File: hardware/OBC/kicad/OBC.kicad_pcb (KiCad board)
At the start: 2 copper layers, 69.5 x 69.5 mm, 37 parts, among them J1 SOCKET_UP, J12 PLACA, J13 Conn_01x08_SocketMPU, J14 Conn_01x04_Socket, J15 Screw_Terminal_01x02, J16 Conn_01x02, J17 Conn_01x06_Socket, J18 Conn_01x02, J19 Conn_01x03, J21 Conn_01x02, J4 PLACA, J7 HEADER_DOWN, J8 PLACA, SW1 SW_SPDT, U1 25CSM04xxSN

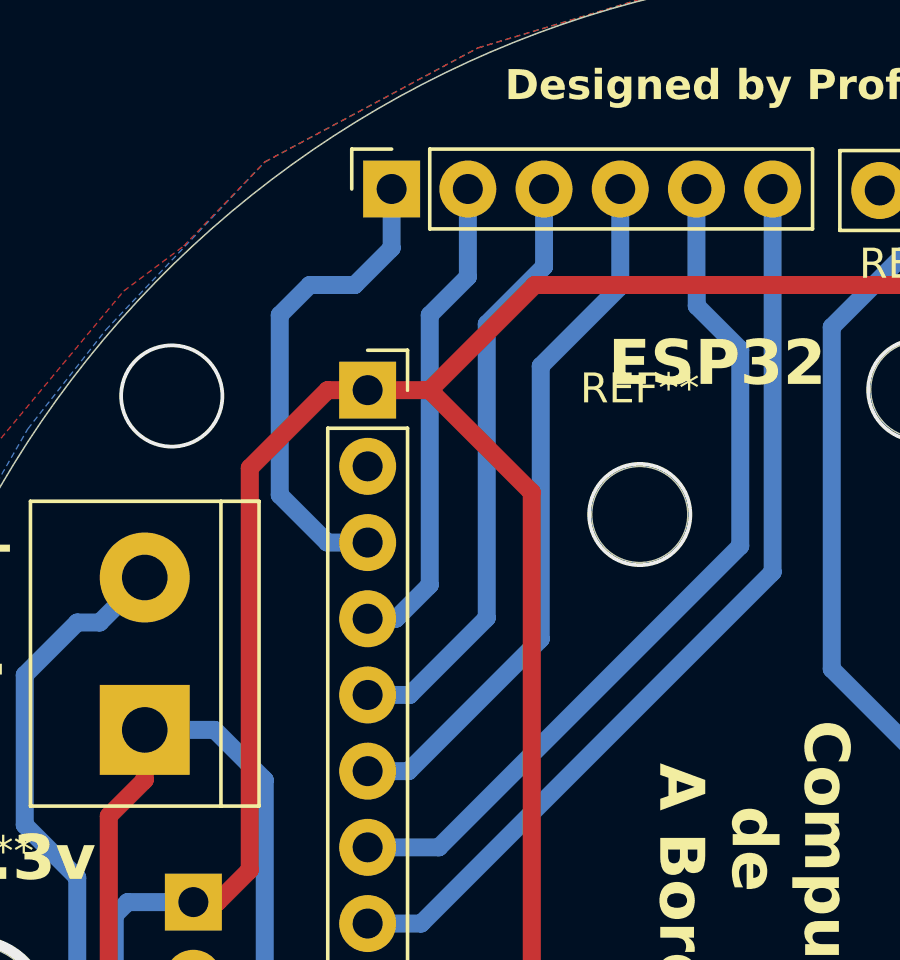
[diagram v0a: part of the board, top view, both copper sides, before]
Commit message: First actualization for OBC PCB
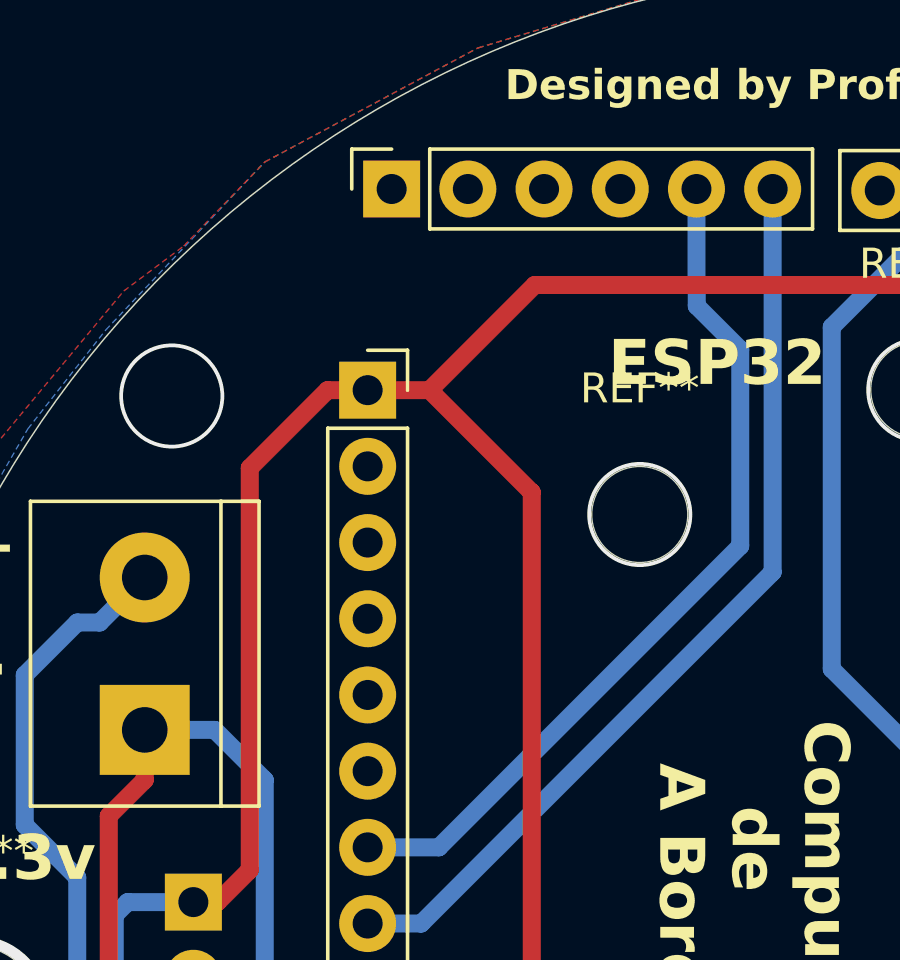
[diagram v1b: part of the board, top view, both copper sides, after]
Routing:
- net GPIO35: track 23.7 -> 0.00 mm
- net GPIO34: track 20.1 -> 0.00 mm
- net GPIO39: track 16.3 -> 0.00 mm
- net GPIO36: track 16.2 -> 0.00 mm
